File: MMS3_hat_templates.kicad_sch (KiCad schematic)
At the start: 9 parts

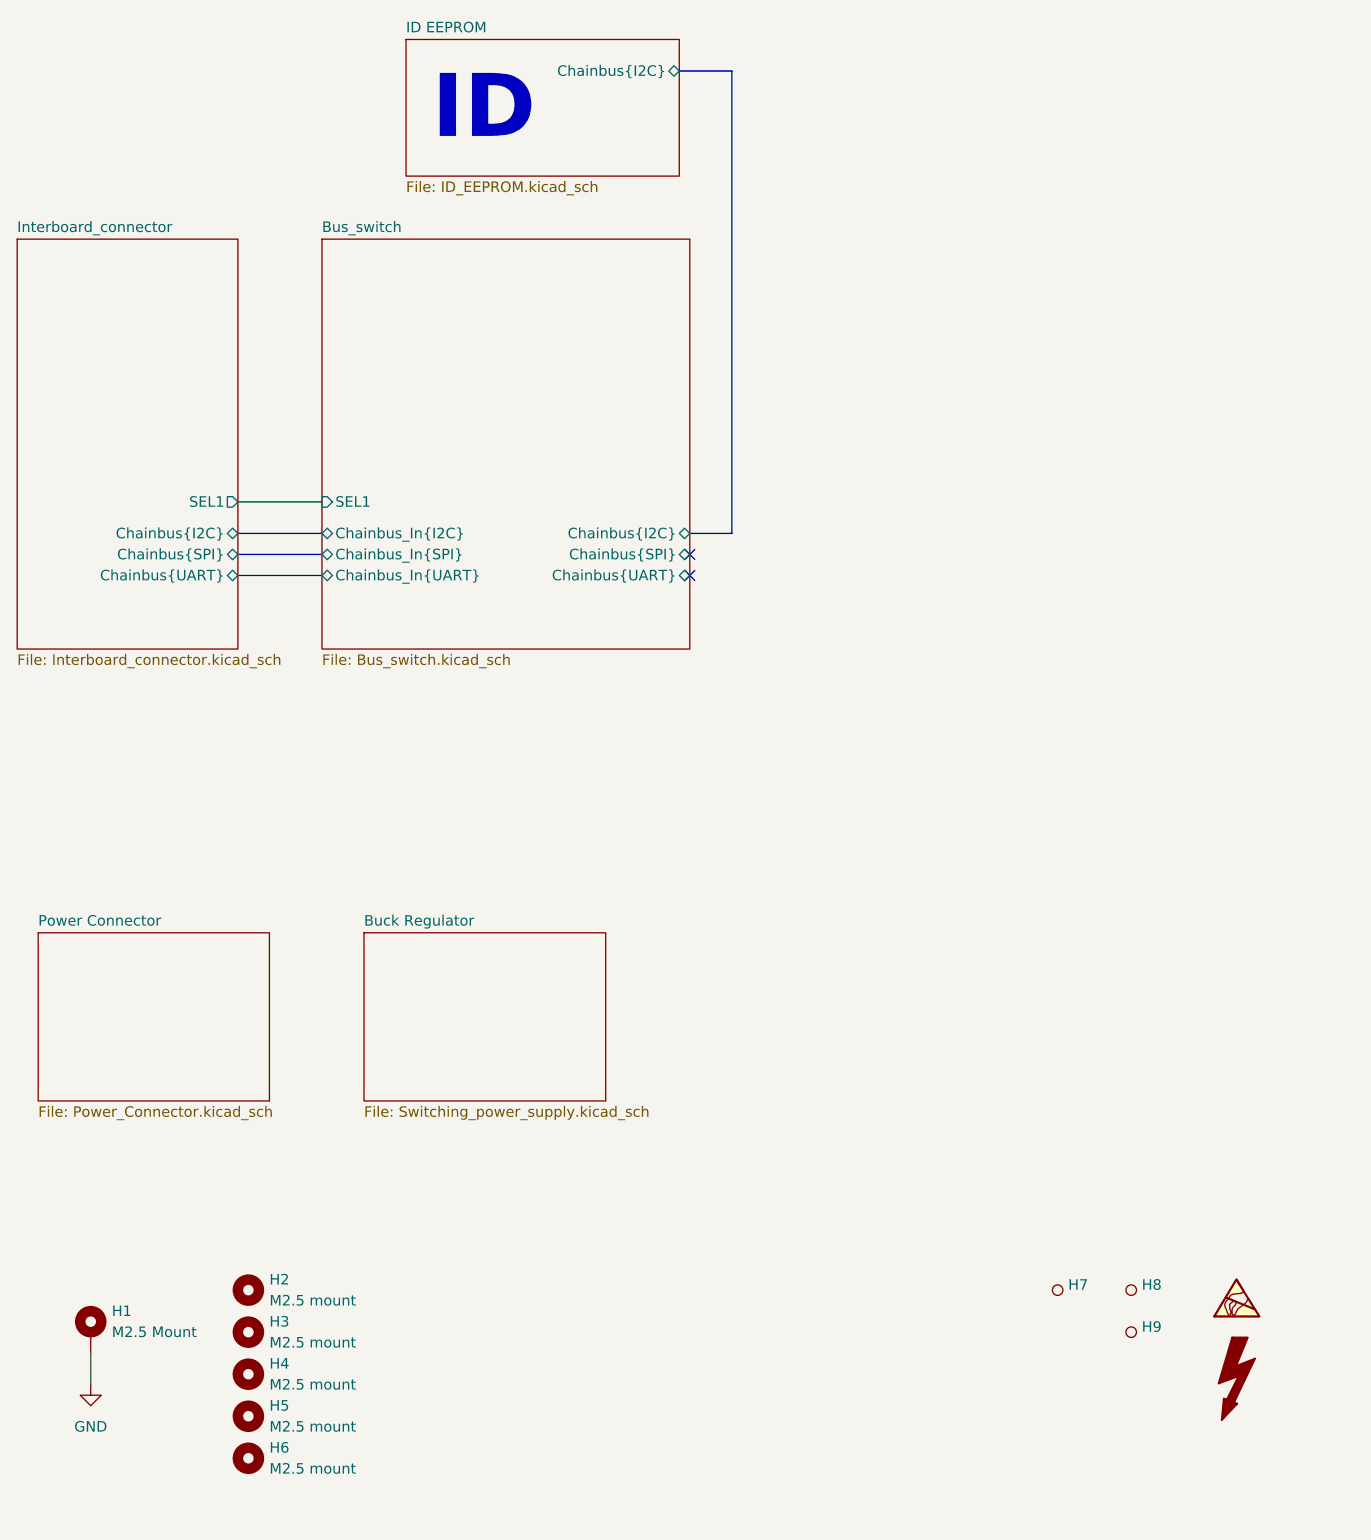
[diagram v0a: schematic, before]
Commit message: ServoController
Dodano arkusz sterownika servo, aktualizacja polaczen
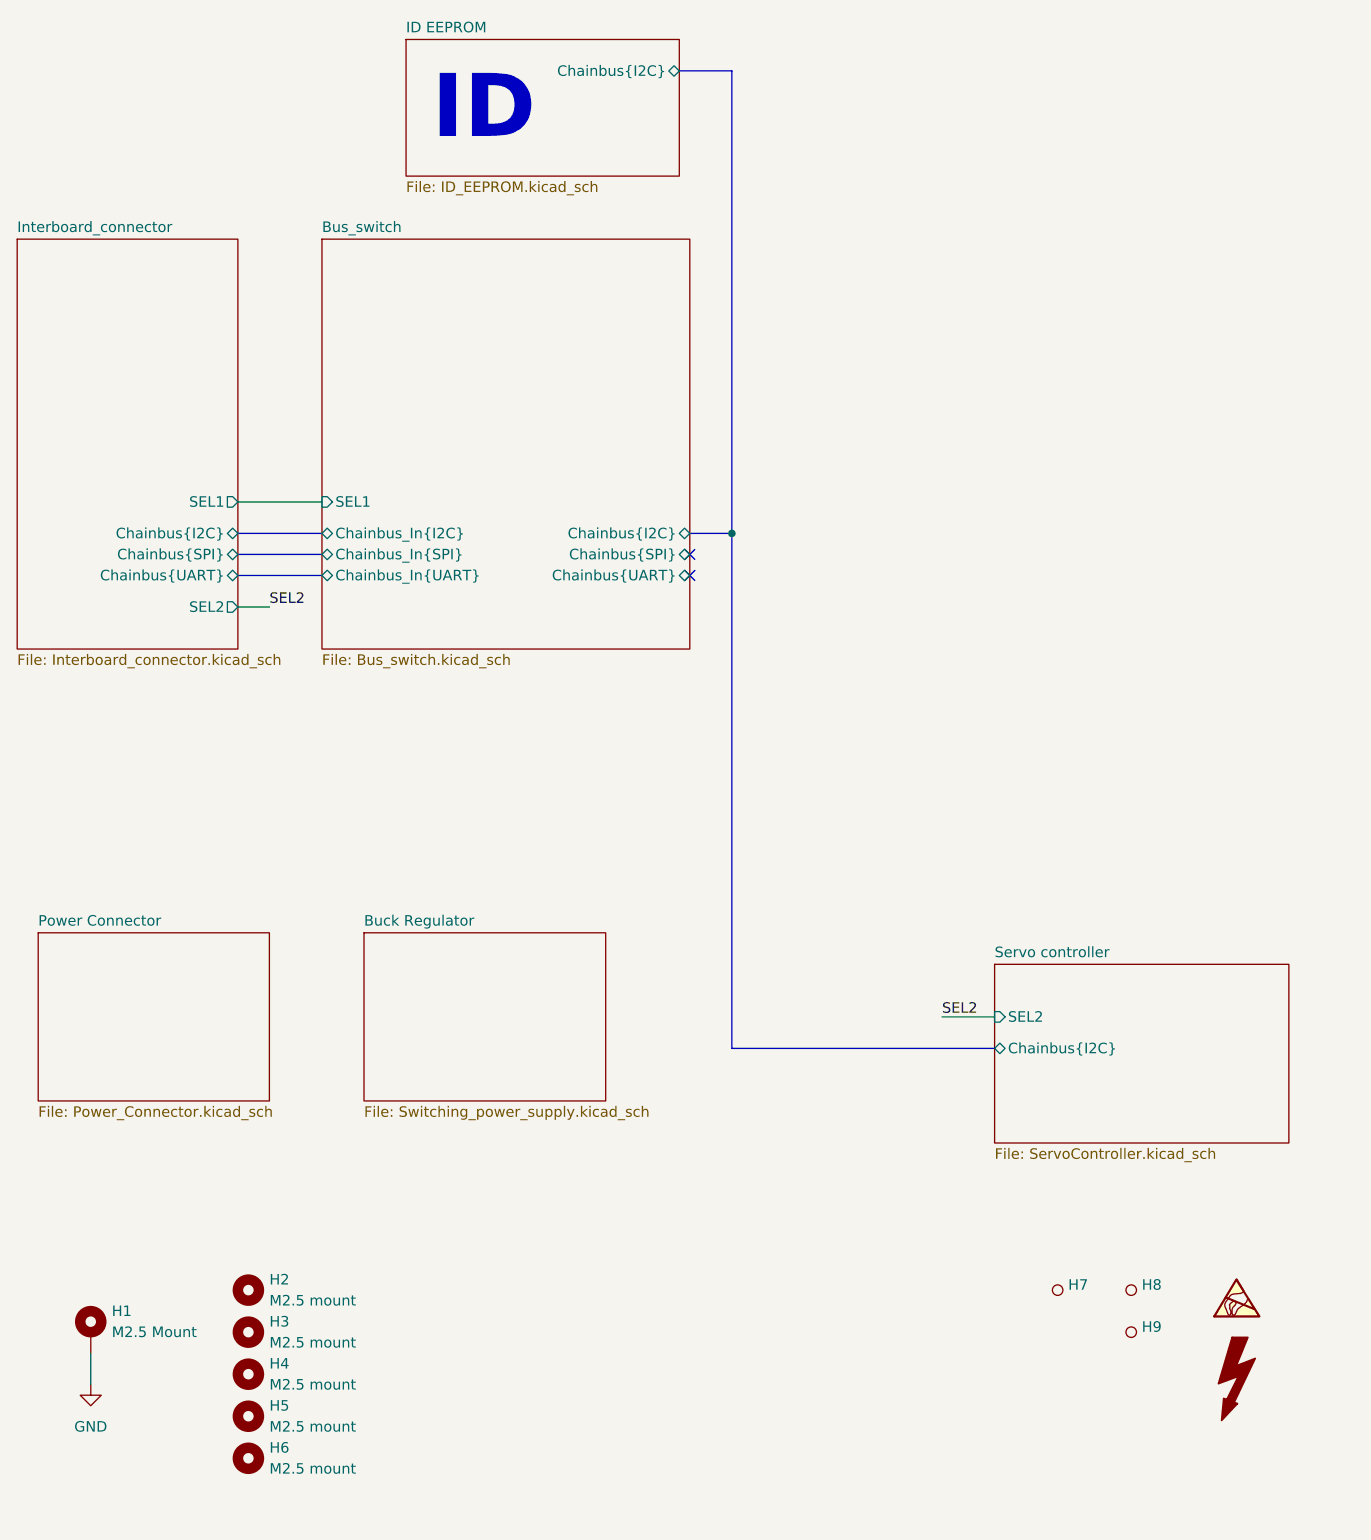
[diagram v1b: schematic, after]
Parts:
- H7, H8, H9: value ~ -> (none)
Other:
- added sheet Servo controller (ServoController.kicad_sch)
- sheet Interboard_connector ports: added SEL2; removed none

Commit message: polished the schemtic
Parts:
- removed H7, H8, H9: (no value), PCM_JLCPCB:Hole_Tooling_JLCPCB, symbol PCM_JLCPCB-Manufacturing:Tooling Hole, PCM_JLCPCB, 1.152mm
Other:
- removed sheet Buck Regulator
- sheet Interboard_connector ports: added none; removed SEL2
- sheet Power Connector ports: added VIN_BRD, VIN_Chainbus; removed none
- sheet Servo controller ports: added Servo_VCC; removed SEL2

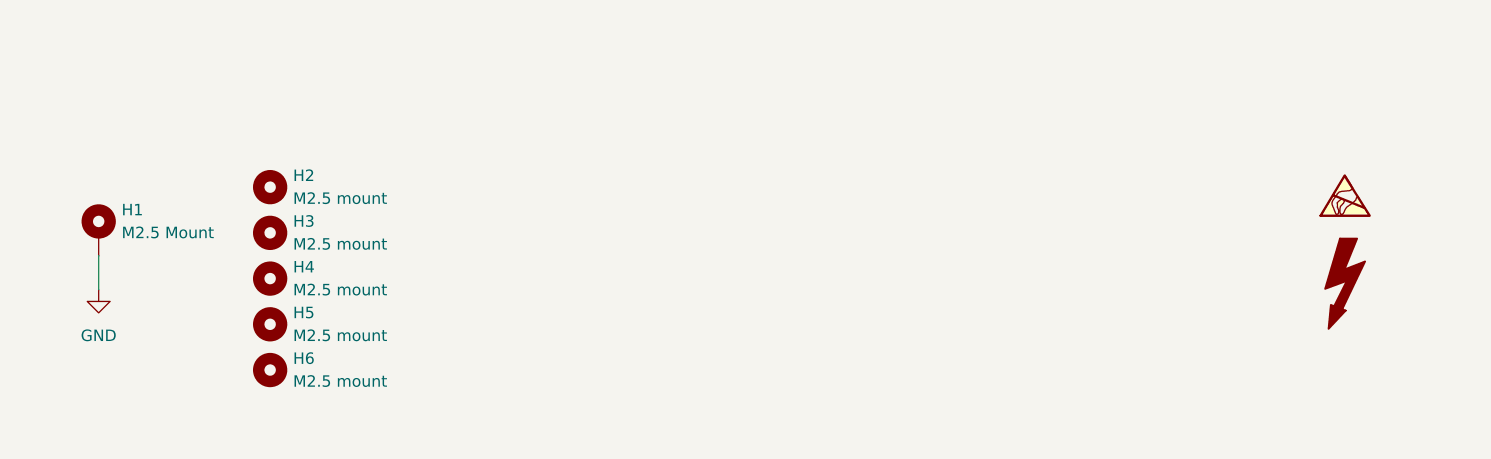
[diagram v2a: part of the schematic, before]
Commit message: added 5V i2c shifter
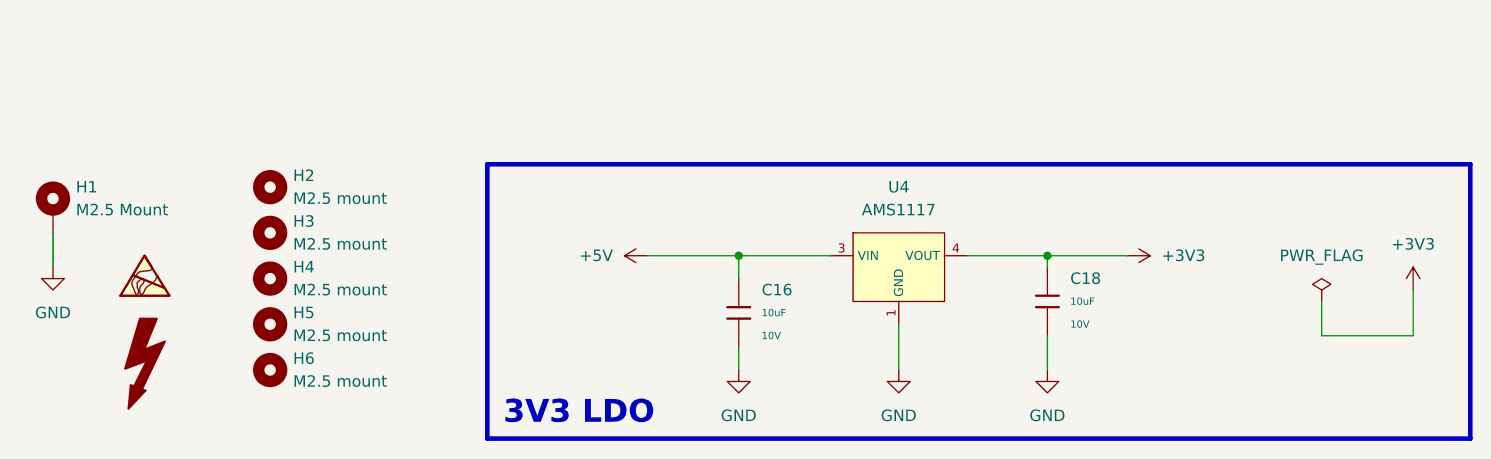
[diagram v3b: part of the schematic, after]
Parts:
- added C16, C18: 10uF, PCM_JLCPCB:C_0603, symbol PCM_JLCPCB-Capacitors:0603,10uF
- added U4: AMS1117, PCM_JLCPCB:SOT-223-3_L6.5-W3.4-P2.30-LS7.0-BR, symbol PCM_JLCPCB-Power:LDO, 3.3V, 1A
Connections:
- net GND: now also C16.2, C18.2, U4.1 (GND)
- new net +3V3: C18.1, U4.2 (VOUT), U4.4 (VOUT)
- new net +5V: C16.1, U4.3 (VIN)
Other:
- note added: "3V3 LDO"
- moved on the sheet: H1
